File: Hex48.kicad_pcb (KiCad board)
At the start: 2 copper layers, 78 x 90.5 mm, 30 parts

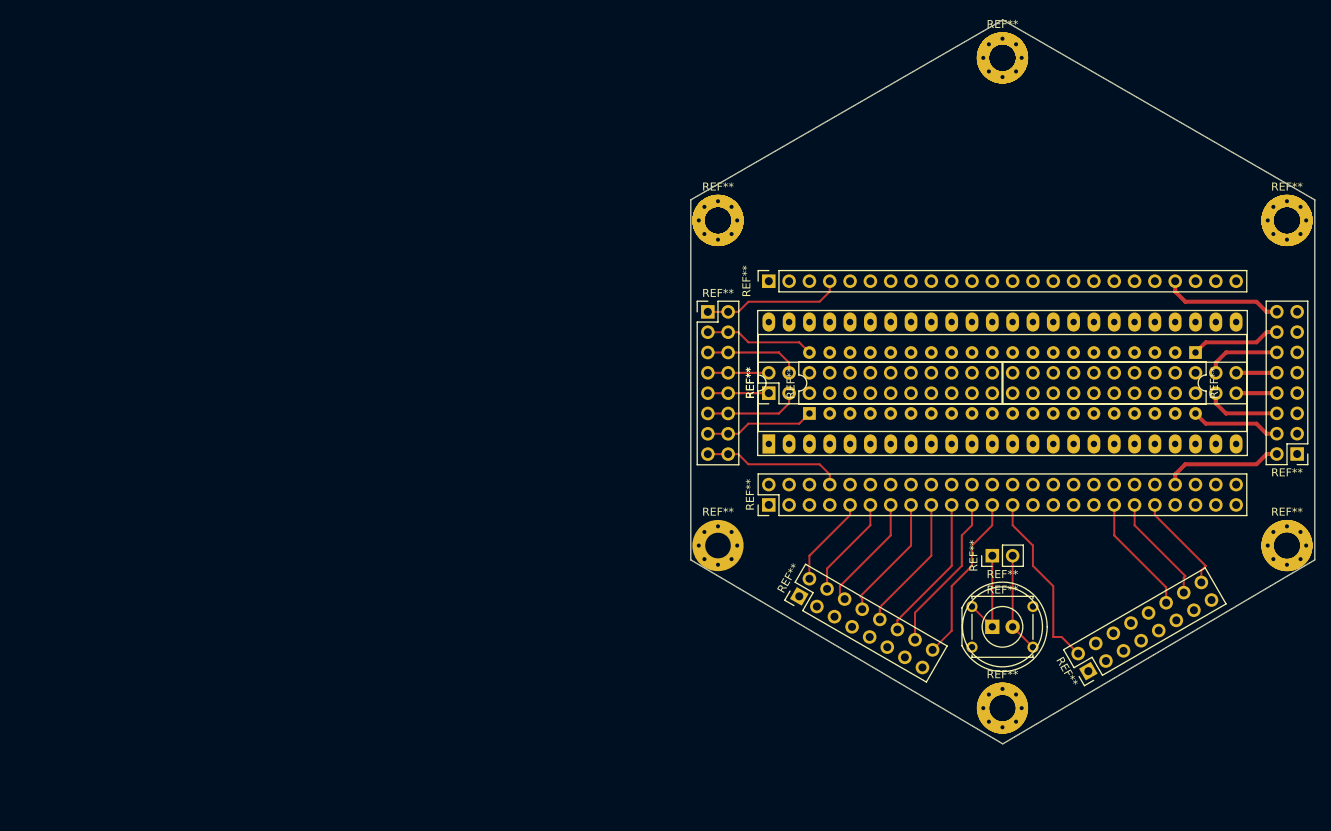
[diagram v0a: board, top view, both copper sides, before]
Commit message: Begin adding schematic.
Board is much better designed by using a proper schematic instead of just a PCB. But to do that, we need lots of generic connectors, all connected together in a way that only makes sense on the physical PCB layout. Oh well, make a start.
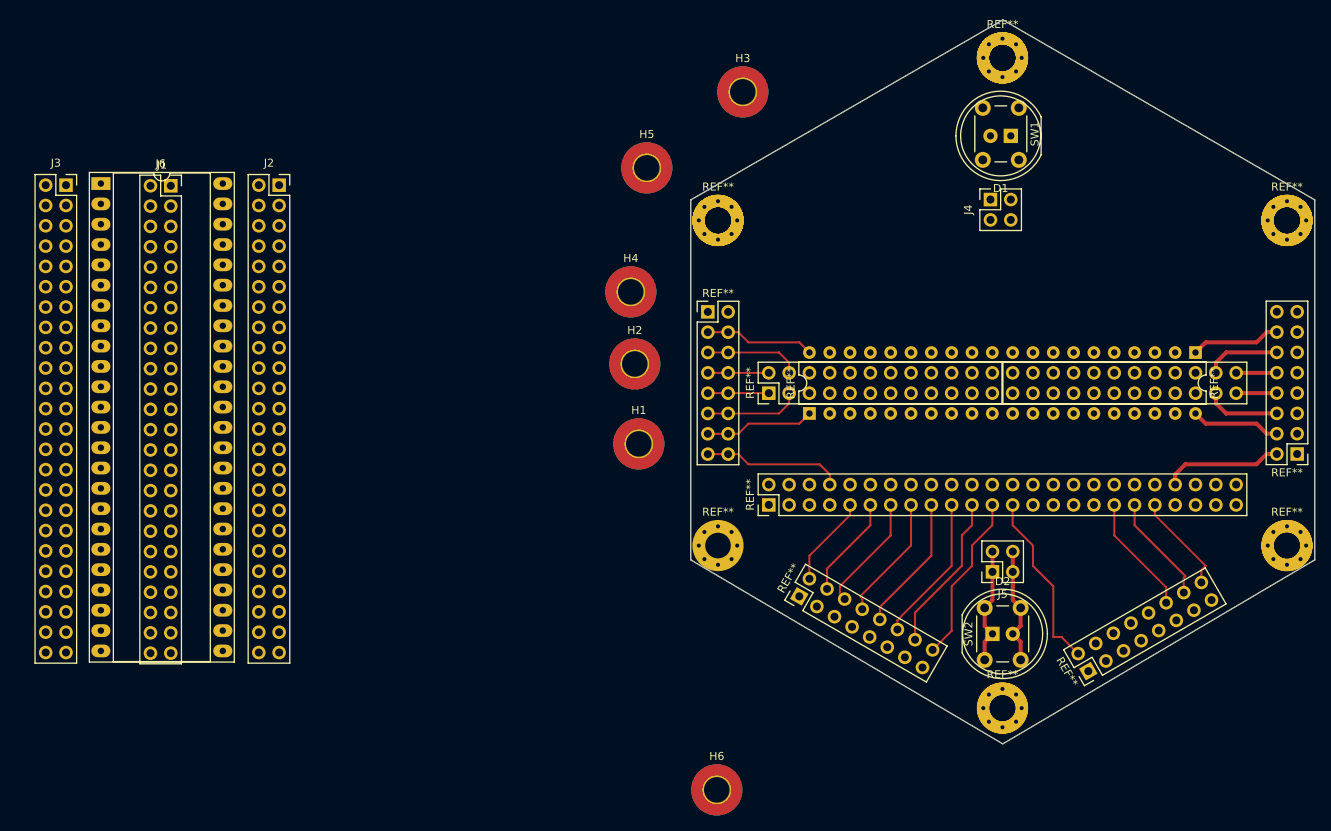
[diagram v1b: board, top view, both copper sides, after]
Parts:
- removed the REF** at (186.7, 94.0)
- removed the REF** at (186.7, 102.9)
- removed the REF** at (184.2, 100.3)
- removed the REF** at (158.8, 80.0)
- removed the REF** at (158.8, 59.7)
- added D1: LED, LED_THT:LED_D10.0mm, F.Cu at (189.0, 41.5)
- added D2: LED, LED_THT:LED_D10.0mm, F.Cu at (186.7, 103.8)
- added H1: MountingHole, MountingHole:MountingHole_3.2mm_M3_Pad_TopBottom, F.Cu at (142.5, 80.0)
- added H2: MountingHole, MountingHole:MountingHole_3.2mm_M3_Pad_TopBottom, F.Cu at (142.0, 70.0)
- added H3: MountingHole, MountingHole:MountingHole_3.2mm_M3_Pad_TopBottom, F.Cu at (155.5, 36.0)
- added H4: MountingHole, MountingHole:MountingHole_3.2mm_M3_Pad_TopBottom, F.Cu at (141.5, 61.0)
- added H5: MountingHole, MountingHole:MountingHole_3.2mm_M3_Pad_TopBottom, F.Cu at (143.5, 45.5)
- added H6: MountingHole, MountingHole:MountingHole_3.2mm_M3_Pad_TopBottom, F.Cu at (152.2, 123.2)
- added J1: Conn_02x24_Counter_Clockwise, Package_DIP:DIP-48_W15.24mm_Socket_LongPads, F.Cu at (75.3, 47.5)
- added J2: Conn_02x24_Odd_Even, Connector_PinSocket_2.54mm:PinSocket_2x24_P2.54mm_Vertical, F.Cu at (97.5, 47.7)
- added J3: Conn_02x24_Odd_Even, Connector_PinSocket_2.54mm:PinSocket_2x24_P2.54mm_Vertical, F.Cu at (70.9, 47.7)
- added J4: Conn_02x02_Odd_Even, Connector_PinSocket_2.54mm:PinSocket_2x02_P2.54mm_Vertical, F.Cu at (186.5, 49.5)
- added J5: Conn_02x02_Odd_Even, Connector_PinSocket_2.54mm:PinSocket_2x02_P2.54mm_Vertical, F.Cu at (186.7, 96.0)
- added J6: Conn_02x24_Odd_Even, Connector_PinSocket_2.54mm:PinSocket_2x24_P2.54mm_Vertical, F.Cu at (84.0, 47.7)
- added SW1: SW_Push, Button_Switch_THT:SW_PUSH_6mm, F.Cu at (190.0, 38.0)
- added SW2: SW_Push, Button_Switch_THT:SW_PUSH_6mm, F.Cu at (185.7, 107.0)
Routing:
- net (no net): track 403.7 -> 302.2 mm
- net Net-(D2-A): track 0.00 -> 58.6 mm
- net Net-(D2-K): track 0.00 -> 15.8 mm

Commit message: Finish DIL wiring.
Place two 24-pin narrow DIL sockets and connect them to the 48-pin wide DIL socket. Name all pin signals.
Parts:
- added J7: Conn_02x12_Counter_Clockwise, Package_DIP:DIP-24_W7.62mm_Socket_LongPads, F.Cu at (78.8, 49.5)
- added J8: Conn_02x12_Counter_Clockwise, Package_DIP:DIP-24_W7.62mm_Socket_LongPads, F.Cu at (78.7, 80.0)
- moved H6 19.5 mm to (133.4, 118.1)
- moved J3 2.98 mm to (68.6, 49.5)
- moved J2 2.41 mm to (99.1, 49.5)
- moved J1 2.10 mm to (74.9, 49.5)
- moved J6 1.80 mm to (83.8, 49.5)
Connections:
- J1 pad 10: Net-(J1-Pin_10) -> /pin10
- J1 pad 11: Net-(J1-Pin_11) -> /pin11
- J1 pad 12: Net-(J1-Pin_12) -> /pin12
- J1 pad 13: Net-(J1-Pin_13) -> /pin13
- J1 pad 14: Net-(J1-Pin_14) -> /pin14
- J1 pad 15: Net-(J1-Pin_15) -> /pin15
- J1 pad 16: Net-(J1-Pin_16) -> /pin16
- J1 pad 17: Net-(J1-Pin_17) -> /pin17
- J1 pad 18: Net-(J1-Pin_18) -> /pin18
- J1 pad 19: Net-(J1-Pin_19) -> /pin19
- J1 pad 20: Net-(J1-Pin_20) -> /pin20
- J1 pad 21: Net-(J1-Pin_21) -> /pin21
- J1 pad 22: Net-(J1-Pin_22) -> /pin22
- J1 pad 23: Net-(J1-Pin_23) -> /pin23
- J1 pad 24: Net-(J1-Pin_24) -> /pin24
- J1 pad 25: Net-(J1-Pin_25) -> /pin25
- J1 pad 26: Net-(J1-Pin_26) -> /pin26
- J1 pad 27: Net-(J1-Pin_27) -> /pin27
- J1 pad 28: Net-(J1-Pin_28) -> /pin28
- J1 pad 29: Net-(J1-Pin_29) -> /pin29
- J1 pad 30: Net-(J1-Pin_30) -> /pin30
- J1 pad 31: Net-(J1-Pin_31) -> /pin31
- J1 pad 32: Net-(J1-Pin_32) -> /pin32
- J1 pad 33: Net-(J1-Pin_33) -> /pin33
- J1 pad 34: Net-(J1-Pin_34) -> /pin34
- J1 pad 35: Net-(J1-Pin_35) -> /pin35
- J1 pad 36: Net-(J1-Pin_36) -> /pin36
- J1 pad 37: Net-(J1-Pin_37) -> /pin37
- J1 pad 38: Net-(J1-Pin_38) -> /pin38
- J1 pad 39: Net-(J1-Pin_39) -> /pin39
- J1 pad 40: Net-(J1-Pin_40) -> /pin40
- J1 pad 9: Net-(J1-Pin_9) -> /pin9
- J2 pad 17: Net-(J1-Pin_40) -> /pin40
- J2 pad 18: Net-(J1-Pin_40) -> /pin40
- J2 pad 19: Net-(J1-Pin_39) -> /pin39
- J2 pad 20: Net-(J1-Pin_39) -> /pin39
- J2 pad 21: Net-(J1-Pin_38) -> /pin38
- J2 pad 22: Net-(J1-Pin_38) -> /pin38
- J2 pad 23: Net-(J1-Pin_37) -> /pin37
- J2 pad 24: Net-(J1-Pin_37) -> /pin37
- J2 pad 25: Net-(J1-Pin_36) -> /pin36
- J2 pad 26: Net-(J1-Pin_36) -> /pin36
- J2 pad 27: Net-(J1-Pin_35) -> /pin35
- J2 pad 28: Net-(J1-Pin_35) -> /pin35
- J2 pad 29: Net-(J1-Pin_34) -> /pin34
- J2 pad 30: Net-(J1-Pin_34) -> /pin34
- J2 pad 31: Net-(J1-Pin_33) -> /pin33
- J2 pad 32: Net-(J1-Pin_33) -> /pin33
- J2 pad 33: Net-(J1-Pin_32) -> /pin32
- J2 pad 34: Net-(J1-Pin_32) -> /pin32
- J2 pad 35: Net-(J1-Pin_31) -> /pin31
- J2 pad 36: Net-(J1-Pin_31) -> /pin31
- J2 pad 37: Net-(J1-Pin_30) -> /pin30
- J2 pad 38: Net-(J1-Pin_30) -> /pin30
- J2 pad 39: Net-(J1-Pin_29) -> /pin29
- J2 pad 40: Net-(J1-Pin_29) -> /pin29
- J2 pad 41: Net-(J1-Pin_28) -> /pin28
- J2 pad 42: Net-(J1-Pin_28) -> /pin28
- J2 pad 43: Net-(J1-Pin_27) -> /pin27
- J2 pad 44: Net-(J1-Pin_27) -> /pin27
- J2 pad 45: Net-(J1-Pin_26) -> /pin26
- J2 pad 46: Net-(J1-Pin_26) -> /pin26
- J2 pad 47: Net-(J1-Pin_25) -> /pin25
- J2 pad 48: Net-(J1-Pin_25) -> /pin25
- J3 pad 17: Net-(J1-Pin_9) -> /pin9
- J3 pad 18: Net-(J1-Pin_9) -> /pin9
- J3 pad 19: Net-(J1-Pin_10) -> /pin10
- J3 pad 20: Net-(J1-Pin_10) -> /pin10
- J3 pad 21: Net-(J1-Pin_11) -> /pin11
- J3 pad 22: Net-(J1-Pin_11) -> /pin11
- J3 pad 23: Net-(J1-Pin_12) -> /pin12
- J3 pad 24: Net-(J1-Pin_12) -> /pin12
- J3 pad 25: Net-(J1-Pin_13) -> /pin13
- J3 pad 26: Net-(J1-Pin_13) -> /pin13
- J3 pad 27: Net-(J1-Pin_14) -> /pin14
- J3 pad 28: Net-(J1-Pin_14) -> /pin14
- J3 pad 29: Net-(J1-Pin_15) -> /pin15
- J3 pad 30: Net-(J1-Pin_15) -> /pin15
- J3 pad 31: Net-(J1-Pin_16) -> /pin16
- J3 pad 32: Net-(J1-Pin_16) -> /pin16
- J3 pad 33: Net-(J1-Pin_17) -> /pin17
- J3 pad 34: Net-(J1-Pin_17) -> /pin17
- J3 pad 35: Net-(J1-Pin_18) -> /pin18
- J3 pad 36: Net-(J1-Pin_18) -> /pin18
- J3 pad 37: Net-(J1-Pin_19) -> /pin19
- J3 pad 38: Net-(J1-Pin_19) -> /pin19
- J3 pad 39: Net-(J1-Pin_20) -> /pin20
- J3 pad 40: Net-(J1-Pin_20) -> /pin20
- J3 pad 41: Net-(J1-Pin_21) -> /pin21
- J3 pad 42: Net-(J1-Pin_21) -> /pin21
- J3 pad 43: Net-(J1-Pin_22) -> /pin22
- J3 pad 44: Net-(J1-Pin_22) -> /pin22
- J3 pad 45: Net-(J1-Pin_23) -> /pin23
- J3 pad 46: Net-(J1-Pin_23) -> /pin23
- J3 pad 47: Net-(J1-Pin_24) -> /pin24
- J3 pad 48: Net-(J1-Pin_24) -> /pin24
- J6 pad 17: unconnected-(J6-Pin_17-Pad17) -> /pin40
- J6 pad 18: unconnected-(J6-Pin_18-Pad18) -> /pin9
- J6 pad 19: unconnected-(J6-Pin_19-Pad19) -> /pin39
- J6 pad 20: unconnected-(J6-Pin_20-Pad20) -> /pin10
- J6 pad 21: unconnected-(J6-Pin_21-Pad21) -> /pin38
- J6 pad 22: unconnected-(J6-Pin_22-Pad22) -> /pin11
- J6 pad 23: unconnected-(J6-Pin_23-Pad23) -> /pin37
- J6 pad 24: unconnected-(J6-Pin_24-Pad24) -> /pin12
- J6 pad 25: unconnected-(J6-Pin_25-Pad25) -> /pin36
- J6 pad 26: unconnected-(J6-Pin_26-Pad26) -> /pin13
- J6 pad 27: unconnected-(J6-Pin_27-Pad27) -> /pin35
- J6 pad 28: unconnected-(J6-Pin_28-Pad28) -> /pin14
- J6 pad 29: unconnected-(J6-Pin_29-Pad29) -> /pin34
- J6 pad 30: unconnected-(J6-Pin_30-Pad30) -> /pin15
- J6 pad 31: unconnected-(J6-Pin_31-Pad31) -> /pin33
- J6 pad 32: unconnected-(J6-Pin_32-Pad32) -> /pin16
- J6 pad 33: unconnected-(J6-Pin_33-Pad33) -> /pin32
- J6 pad 34: unconnected-(J6-Pin_34-Pad34) -> /pin17
- J6 pad 35: unconnected-(J6-Pin_35-Pad35) -> /pin31
- J6 pad 36: unconnected-(J6-Pin_36-Pad36) -> /pin18
- J6 pad 37: unconnected-(J6-Pin_37-Pad37) -> /pin30
- J6 pad 38: unconnected-(J6-Pin_38-Pad38) -> /pin19
- J6 pad 39: unconnected-(J6-Pin_39-Pad39) -> /pin29
- J6 pad 40: unconnected-(J6-Pin_40-Pad40) -> /pin20
- J6 pad 41: unconnected-(J6-Pin_41-Pad41) -> /pin28
- J6 pad 42: unconnected-(J6-Pin_42-Pad42) -> /pin21
- J6 pad 43: unconnected-(J6-Pin_43-Pad43) -> /pin27
- J6 pad 44: unconnected-(J6-Pin_44-Pad44) -> /pin22
- J6 pad 45: unconnected-(J6-Pin_45-Pad45) -> /pin26
- J6 pad 46: unconnected-(J6-Pin_46-Pad46) -> /pin23
- J6 pad 47: unconnected-(J6-Pin_47-Pad47) -> /pin25
- J6 pad 48: unconnected-(J6-Pin_48-Pad48) -> /pin24
